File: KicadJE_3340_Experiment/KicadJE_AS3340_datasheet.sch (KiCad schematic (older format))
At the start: 43 parts, among them J201 In1.1, J202 In1.2, J203 In1.3, J204 RampOut1, J205 SS_In2, J206 PulseOut2, J207 SawOut3, SW201 Inv/NonInv, SW202 Inv/NonInv, U201 TL082

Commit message: two sub sheets made ready
incomplete
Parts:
- added D?: 1N4148, Diode_SMD:D_SOD-123, symbol Device:D
- added R?: 0R, Resistor_SMD:R_0805_2012Metric_Pad1.15x1.40mm_HandSolder, symbol Device:R
- added R?: Open / 300K if lin pot, Resistor_SMD:R_0805_2012Metric_Pad1.15x1.40mm_HandSolder, symbol Device:R
- added R?: 100R, Resistor_SMD:R_0805_2012Metric_Pad1.15x1.40mm_HandSolder, symbol Device:R
- added RV?: 1M Release, AJ-Dropbox-Kicad:Potentiometer_China_RK09_Single_Vertical_AJ, symbol Envelope-cache-2018-08-04-13-00-04:POT
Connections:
- new net: D?.2 (A), R?.1, RV?.1
- new net: R?.2, R?.2, RV?.2
- new net: R?.1, R?.2, RV?.3
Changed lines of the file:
@@
 $Descr A4 11693 8268
 encoding utf-8
-Sheet 2 2
+Sheet 2 3
 Title ""
 Date "2019-03-19"
@@
 Wire Wire Line
 	5425 2700 6250 2700
+$Comp
+L Envelope-cache-2018-08-04-13-00-04:POT RV?
+U 1 1 5E635430
+P 5000 4875
+AR Path="/5D99B7BA/5E635430" Ref="RV?"  Part="1"
+AR Path="/5F18E4B5/5E635430" Ref="RV?"  Part="1"
+AR Path="/5E62ACA1/5E635430" Ref="RV?"  Part="1"
+F 0 "RV?" V 5000 4900 50  0000 C CNN
+F 1 "1M Release" V 4794 4875 50  0000 C CNN
+F 2 "AJ-Dropbox-Kicad:Potentiometer_China_RK09_Single_Vertical_AJ" H 5000 4875 50  0001 C CNN
+F 3 "" H 5000 4875 50  0001 C CNN
+	1    5000 4875
+	0    -1   -1   0
+$EndComp
+Wire Wire Line
+	5150 4875 5200 4875
+Wire Wire Line
+	4800 4725 4800 4875
+Wire Wire Line
+	4800 4875 4850 4875
+$Comp
+L Device:R R?
+U 1 1 5E635439
+P 4800 4575
+AR Path="/5D99B81E/5E635439" Ref="R?"  Part="1"
+AR Path="/5D99B7BA/5E635439" Ref="R?"  Part="1"
+AR Path="/5F18E4B5/5E635439" Ref="R?"  Part="1"
+AR Path="/5E62ACA1/5E635439" Ref="R?"  Part="1"
+F 0 "R?" V 4800 4625 50  0000 C CNN
+F 1 "0R" V 4700 4650 50  0000 C CNN
+F 2 "Resistor_SMD:R_0805_2012Metric_Pad1.15x1.40mm_HandSolder" V 4730 4575 50  0001 C CNN
+F 3 "~" H 4800 4575 50  0001 C CNN
+	1    4800 4575
+	-1   0    0    1
+$EndComp
+$Comp
+L Device:R R?
+U 1 1 5E63543F
+P 5200 4575
+AR Path="/5D99B81E/5E63543F" Ref="R?"  Part="1"
+AR Path="/5D99B7BA/5E63543F" Ref="R?"  Part="1"
+AR Path="/5F18E4B5/5E63543F" Ref="R?"  Part="1"
+AR Path="/5E62ACA1/5E63543F" Ref="R?"  Part="1"
+F 0 "R?" V 5200 4625 50  0000 C CNN
+F 1 "Open / 300K if lin pot" V 5075 4275 50  0000 C CNN
+F 2 "Resistor_SMD:R_0805_2012Metric_Pad1.15x1.40mm_HandSolder" V 5130 4575 50  0001 C CNN
+F 3 "~" H 5200 4575 50  0001 C CNN
+	1    5200 4575
+	-1   0    0    1
+$EndComp
+Wire Wire Line
+	5200 4725 5200 4875
+Wire Wire Line
+	5200 4425 5200 4375
+Wire Wire Line
+	5200 4375 5000 4375
+Wire Wire Line
+	4800 4375 4800 4425
+Wire Wire Line
+	5000 4725 5000 4375
+Connection ~ 5000 4375
+Wire Wire Line
+	5000 4375 4800 4375
+Connection ~ 4800 4875
+Wire Wire Line
+	4575 4875 4800 4875
+$Comp
+L Device:R R?
+U 1 1 5E63544E
+P 5425 4875
+AR Path="/5E63544E" Ref="R?"  Part="1"
+AR Path="/5CD3F059/5E63544E" Ref="R?"  Part="1"
+AR Path="/5CEBAECA/5E63544E" Ref="R?"  Part="1"
+AR Path="/5DD87D87/5DDB8911/5E63544E" Ref="R?"  Part="1"
+AR Path="/5DD87D87/5E63544E" Ref="R?"  Part="1"
+AR Path="/5F18E4B5/5E63544E" Ref="R?"  Part="1"
+AR Path="/5E62ACA1/5E63544E" Ref="R?"  Part="1"
+F 0 "R?" V 5425 4825 50  0000 C CNN
+F 1 "100R" V 5309 4875 50  0000 C CNN
+F 2 "Resistor_SMD:R_0805_2012Metric_Pad1.15x1.40mm_HandSolder" V 5355 4875 50  0001 C CNN
+F 3 "~" H 5425 4875 50  0001 C CNN
+	1    5425 4875
+	0    1    1    0
+$EndComp
+Wire Wire Line
+	5275 4875 5200 4875
+Connection ~ 5200 4875
+$Comp
+L Device:D D?
+U 1 1 5E635456
+P 4425 4875
+AR Path="/5E635456" Ref="D?"  Part="1"
+AR Path="/5D60ED9A/5E635456" Ref="D?"  Part="1"
+AR Path="/5CD6EBF4/5E635456" Ref="D?"  Part="1"
+AR Path="/5CE53731/5E635456" Ref="D?"  Part="1"
+AR Path="/5DD87D87/5E635456" Ref="D?"  Part="1"
+AR Path="/5F18E4B5/5E635456" Ref="D?"  Part="1"
+AR Path="/5E62ACA1/5E635456" Ref="D?"  Part="1"
+F 0 "D?" V 4379 4954 50  0000 L CNN
+F 1 "1N4148" V 4425 4500 50  0000 L CNN
+F 2 "Diode_SMD:D_SOD-123" H 4425 4875 50  0001 C CNN
+F 3 "~" H 4425 4875 50  0001 C CNN
+	1    4425 4875
+	1    0    0    -1
+$EndComp
 $EndSCHEMATC

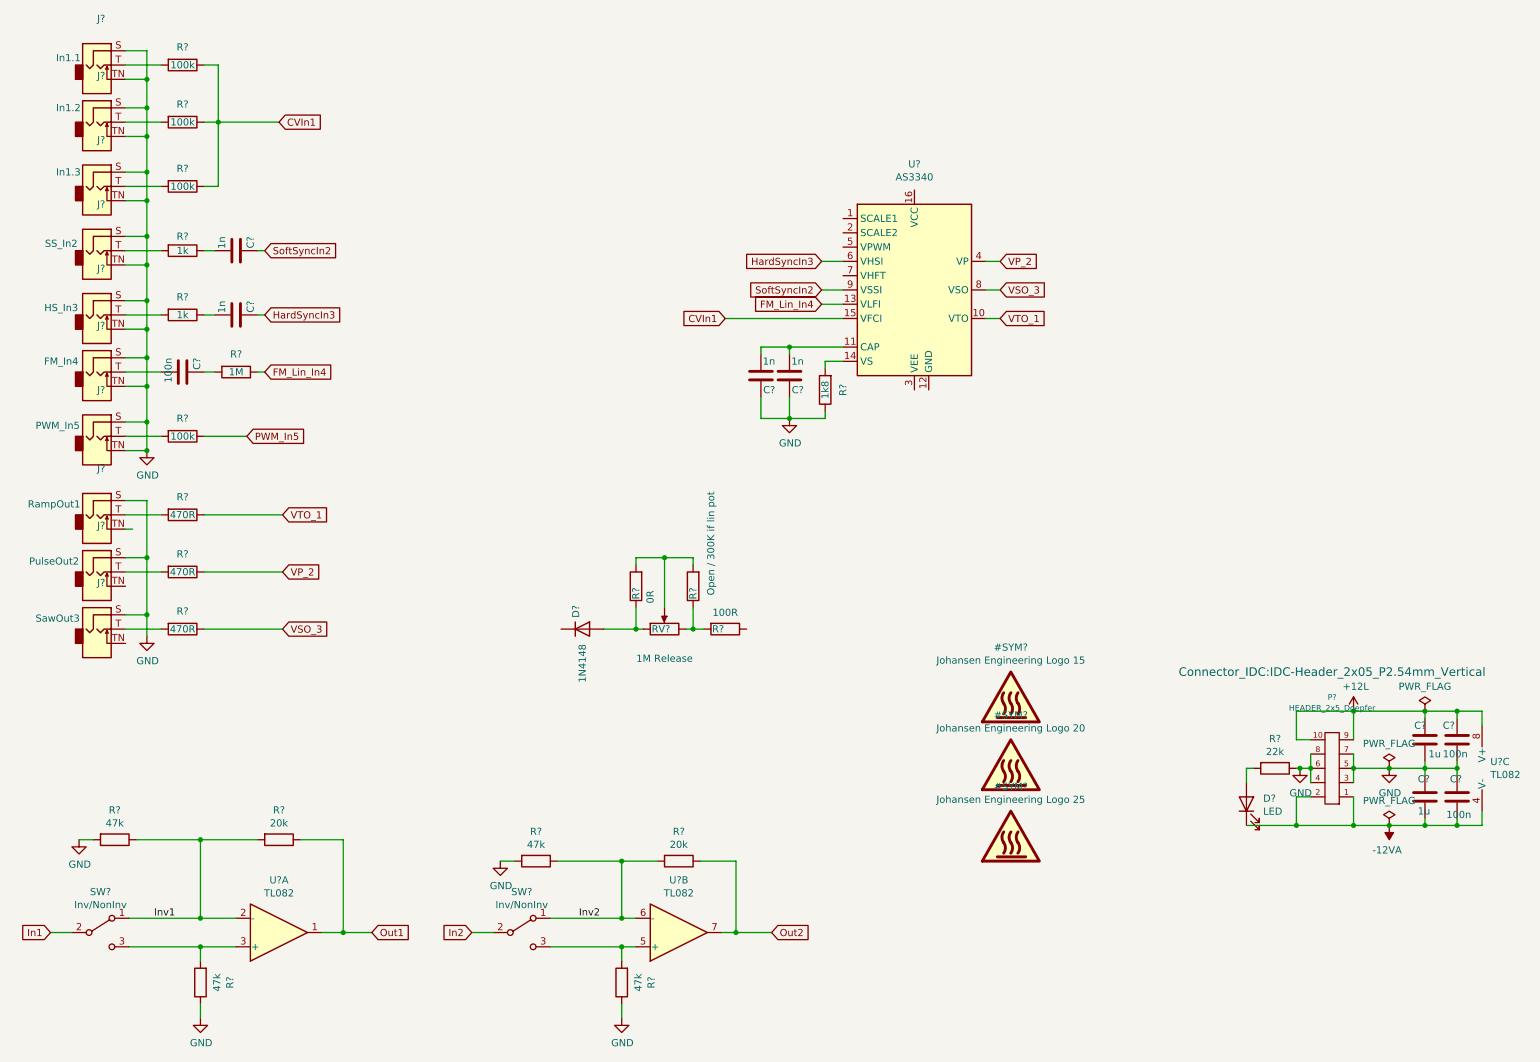
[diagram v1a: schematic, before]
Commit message: Datasheet initial done sch
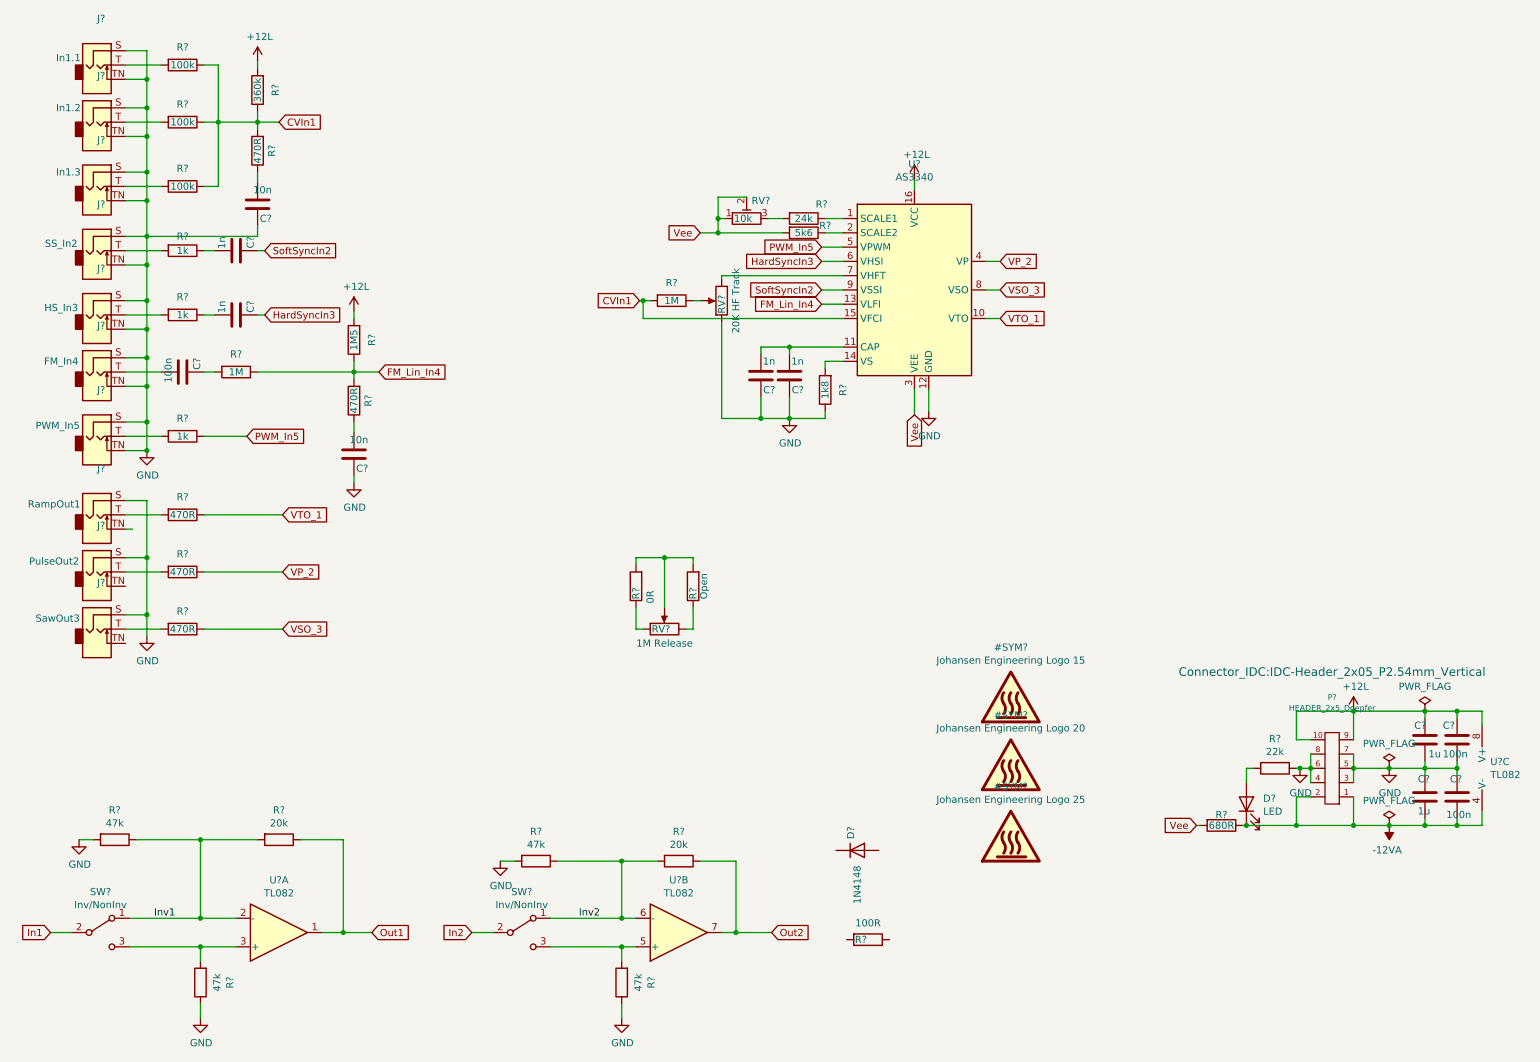
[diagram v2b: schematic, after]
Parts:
- added C? (x2): 10n, Capacitor_SMD:C_0805_2012Metric_Pad1.15x1.40mm_HandSolder, symbol Device:C
- added R?: 1M, Resistor_SMD:R_0805_2012Metric_Pad1.15x1.40mm_HandSolder, symbol Device:R
- added R? (x2): 470R, Resistor_SMD:R_0805_2012Metric_Pad1.15x1.40mm_HandSolder, symbol Device:R
- added R?: 360k, Resistor_SMD:R_0805_2012Metric_Pad1.15x1.40mm_HandSolder, symbol Device:R
- added R?: 5k6, Resistor_SMD:R_0805_2012Metric_Pad1.15x1.40mm_HandSolder, symbol Device:R
- added R?: 24k, Resistor_SMD:R_0805_2012Metric_Pad1.15x1.40mm_HandSolder, symbol Device:R
- added R?: 680R, Resistor_SMD:R_0805_2012Metric_Pad1.15x1.40mm_HandSolder, symbol Device:R
- added R?: 1M5, Resistor_SMD:R_0805_2012Metric_Pad1.15x1.40mm_HandSolder, symbol Device:R
- added RV?: 20K HF Track, AJ-Dropbox-Kicad:Potentiometer_China_RK09_Single_Vertical_AJ, symbol Envelope-cache-2018-08-04-13-00-04:POT
- added RV?: 10k, symbol Device:R_POT_TRIM
- R?: value 100k -> 1k
- R?: value Open / 300K if lin pot -> Open
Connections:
- net +12L: now also U?.16 (VCC), R?.2, R?.2
- net -12VA: now also R?.1
- net CVIn1: now also R?.1, R?.2, R?.2
- net FM_Lin_In4: now also R?.1, R?.2
- net GND: now also U?.12 (GND), C?.1, C?.1, RV?.1
- net PWM_In5: now also U?.5 (VPWM)
- net at U?.1 (SCALE1): now also R?.1
- net at U?.2 (SCALE2): now also R?.1
- net Vee: now reaches U?.3 (VEE)
- net Vee: now also R?.2, R?.2, RV?.1, RV?.2
- net at U?.7 (VHFT): now also RV?.3
- net at R?.1, RV?.1: no longer D?.2 (A)
- net at R?.1, RV?.3: no longer R?.2
- new net: R?.1, RV?.2
- new net: C?.2, R?.1 (x2)
- new net: R?.2, RV?.3
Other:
- moved on the sheet: D?, R?

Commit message: protection initiated
prophet circuit initiated
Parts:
- added C? (x2): 100n, Capacitor_SMD:C_0805_2012Metric_Pad1.15x1.40mm_HandSolder, symbol Device:C
- added C? (x2): 1u, Capacitor_SMD:C_1206_3216Metric_Pad1.42x1.75mm_HandSolder, symbol Device:C
- added D? (x4): 1N1007, Diode_SMD:D_SOD-123, symbol Device:D
- added U?: TL072, AJ-Dropbox-Kicad:AJ_SO-8_5.3x6.2mm_P1.27mm, symbol Amplifier_Operational:TL072
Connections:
- net GND: now also C?.1, C?.1, C?.1, C?.1, D?.1 (K), D?.2 (A), D?.2 (A)
- new net: D?.1 (K), D?.2 (A)
- new net +12V: C?.2, C?.2, D?.1 (K), D?.1 (K), U?.8 (V+)
- new net -12V: C?.2, C?.2, D?.2 (A), U?.4 (V-)
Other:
- moved on the sheet: D?, R?, RV?

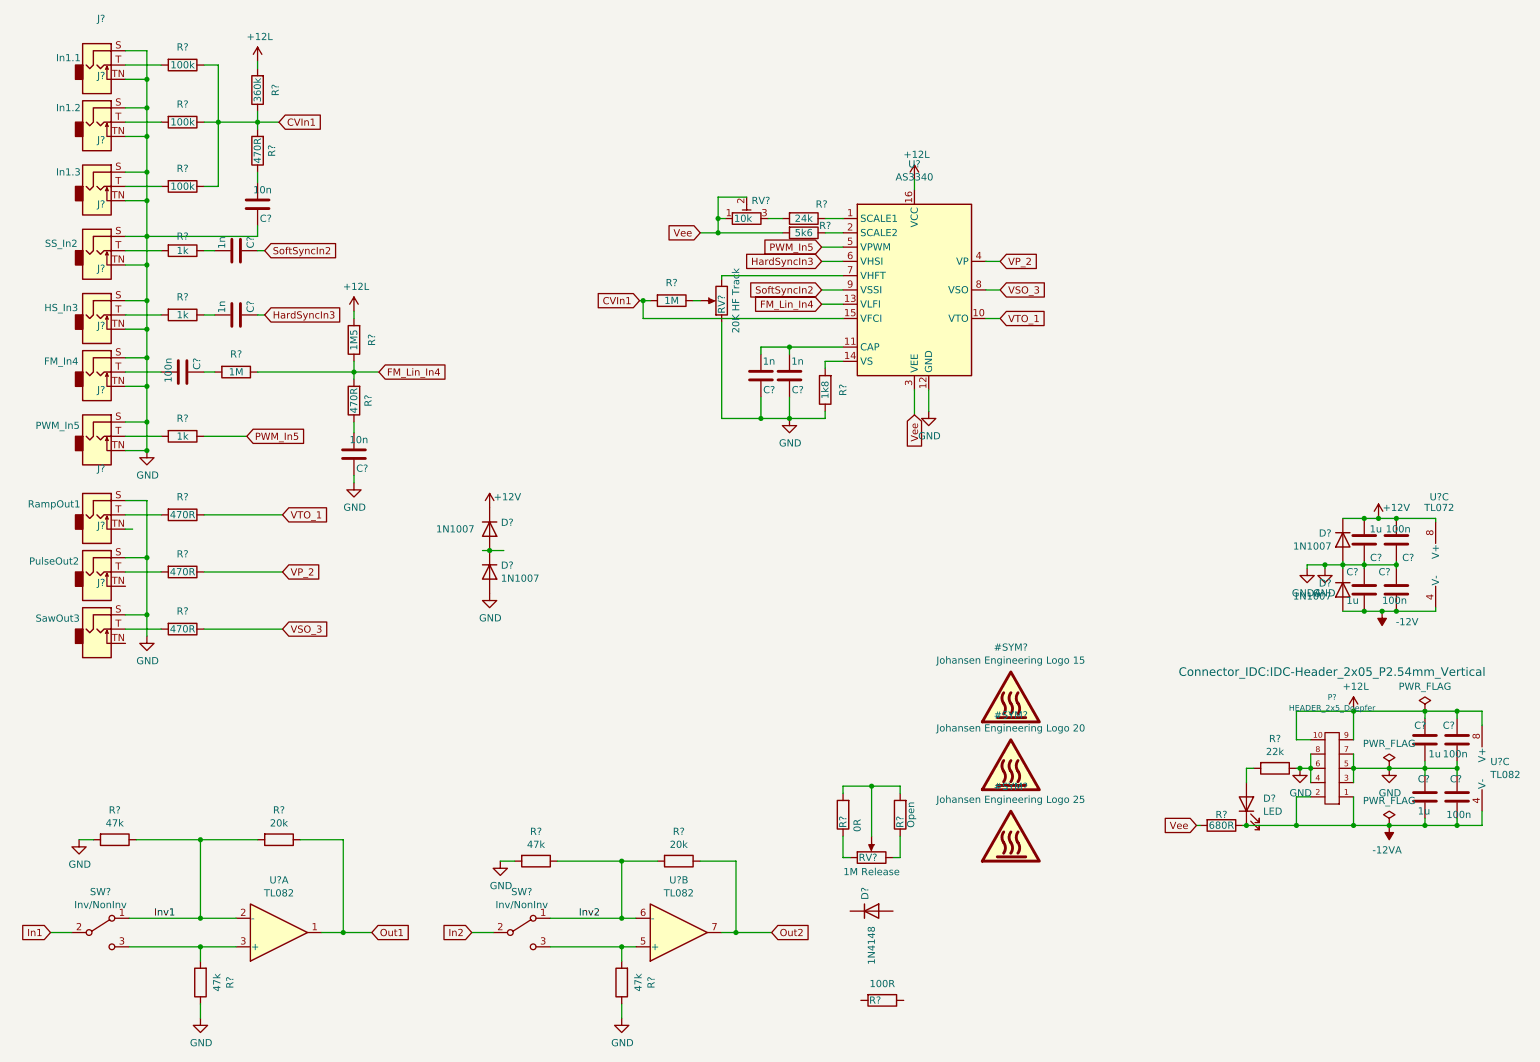
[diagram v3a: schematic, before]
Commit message: Datasheet input protection
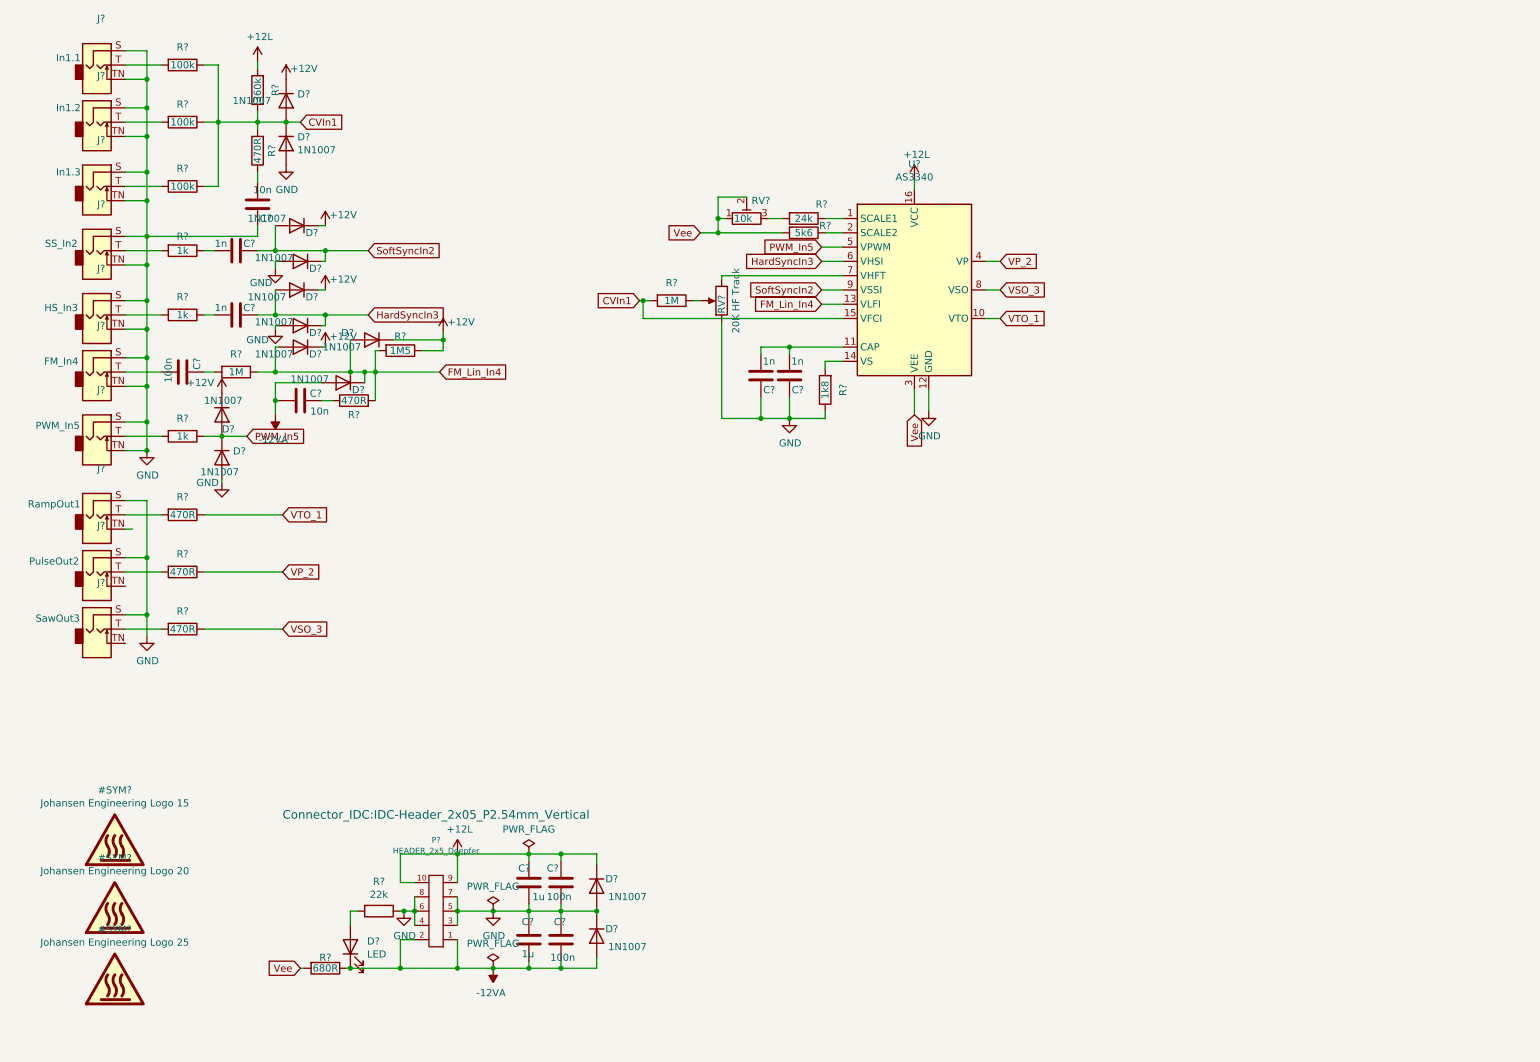
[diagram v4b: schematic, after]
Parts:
- removed C? (x2): 100n, Capacitor_SMD:C_0805_2012Metric_Pad1.15x1.40mm_HandSolder, symbol Device:C
- removed C? (x2): 1u, Capacitor_SMD:C_1206_3216Metric_Pad1.42x1.75mm_HandSolder, symbol Device:C
- removed D?: 1N4148, Diode_SMD:D_SOD-123, symbol Device:D
- removed R201, R206, R208, R212: 47k, Resistor_SMD:R_0805_2012Metric_Pad1.15x1.40mm_HandSolder, symbol Device:R
- removed R202, R209: 20k, Resistor_SMD:R_0805_2012Metric_Pad1.15x1.40mm_HandSolder, symbol Device:R
- removed R?: 0R, Resistor_SMD:R_0805_2012Metric_Pad1.15x1.40mm_HandSolder, symbol Device:R
- removed R?: Open, Resistor_SMD:R_0805_2012Metric_Pad1.15x1.40mm_HandSolder, symbol Device:R
- removed R?: 100R, Resistor_SMD:R_0805_2012Metric_Pad1.15x1.40mm_HandSolder, symbol Device:R
- removed RV?: 1M Release, AJ-Dropbox-Kicad:Potentiometer_China_RK09_Single_Vertical_AJ, symbol Envelope-cache-2018-08-04-13-00-04:POT
- removed SW201, SW202: Inv/NonInv, AJ-Dropbox-Kicad:SP1MS1, symbol Switch:SW_SPDT
- removed U201: TL082, AJ-Dropbox-Kicad:AJ_SO-8_5.3x6.2mm_P1.27mm, symbol Amplifier_Operational:TL082
- removed U?: TL072, AJ-Dropbox-Kicad:AJ_SO-8_5.3x6.2mm_P1.27mm, symbol Amplifier_Operational:TL072
- added D? (x9): 1N1007, Diode_SMD:D_SOD-123, symbol Device:D
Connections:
- net -12V is gone; now on net -12VA: D?.2 (A)
- net +12L: now also D?.1 (K); no longer R?.2
- net +12V: now also R?.1, D?.1 (K), D?.1 (K), D?.1 (K), D?.1 (K), D?.1 (K); no longer D?.1 (K)
- net -12VA: now also C?.1, D?.2 (A)
- net CVIn1: now also D?.1 (K), D?.2 (A)
- net FM_Lin_In4: now also R?.2, D?.1 (K), D?.2 (A), D?.2 (A); no longer R?.1
- net GND: now also D?.2 (A), D?.2 (A), D?.2 (A); no longer C?.1
- net HardSyncIn3: now also D?.1 (K), D?.2 (A)
- net PWM_In5: now also D?.1 (K), D?.2 (A)
- net SoftSyncIn2: now also D?.1 (K), D?.2 (A)
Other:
- moved on the sheet: C?, D?, P?, R?
